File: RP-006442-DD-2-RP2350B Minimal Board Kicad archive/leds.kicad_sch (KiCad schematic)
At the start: 34 parts, among them U10 74HC595, U11 74HC595

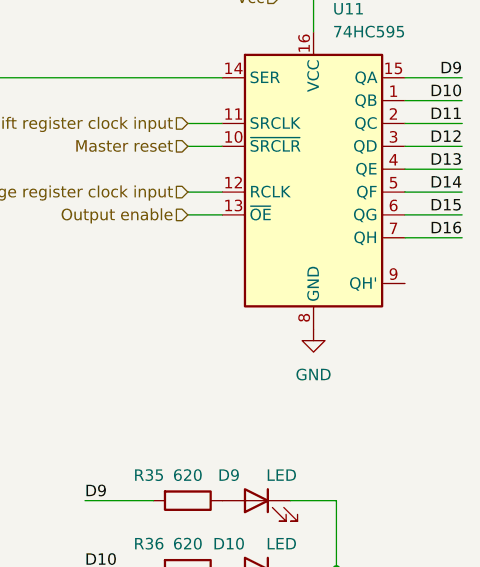
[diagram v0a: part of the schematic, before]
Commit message: Connected GPIOs to Shift Register pins
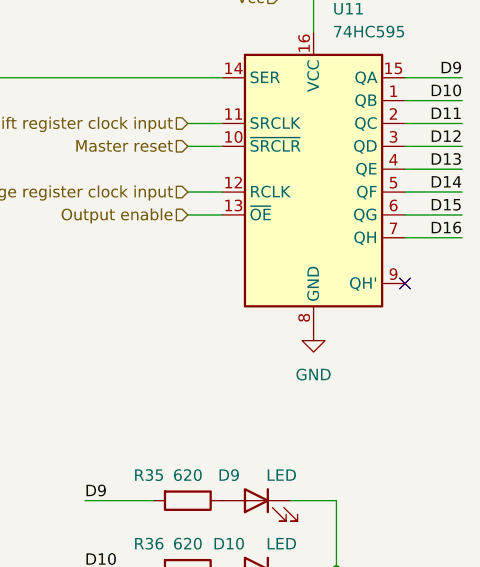
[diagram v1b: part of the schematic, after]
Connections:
- no-connect marks 0 -> 1
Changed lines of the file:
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@@
 		(color 0 0 0 0)
+	)
+	(no_connect
+		(at 162.56 74.93)
 	)
 	(wire

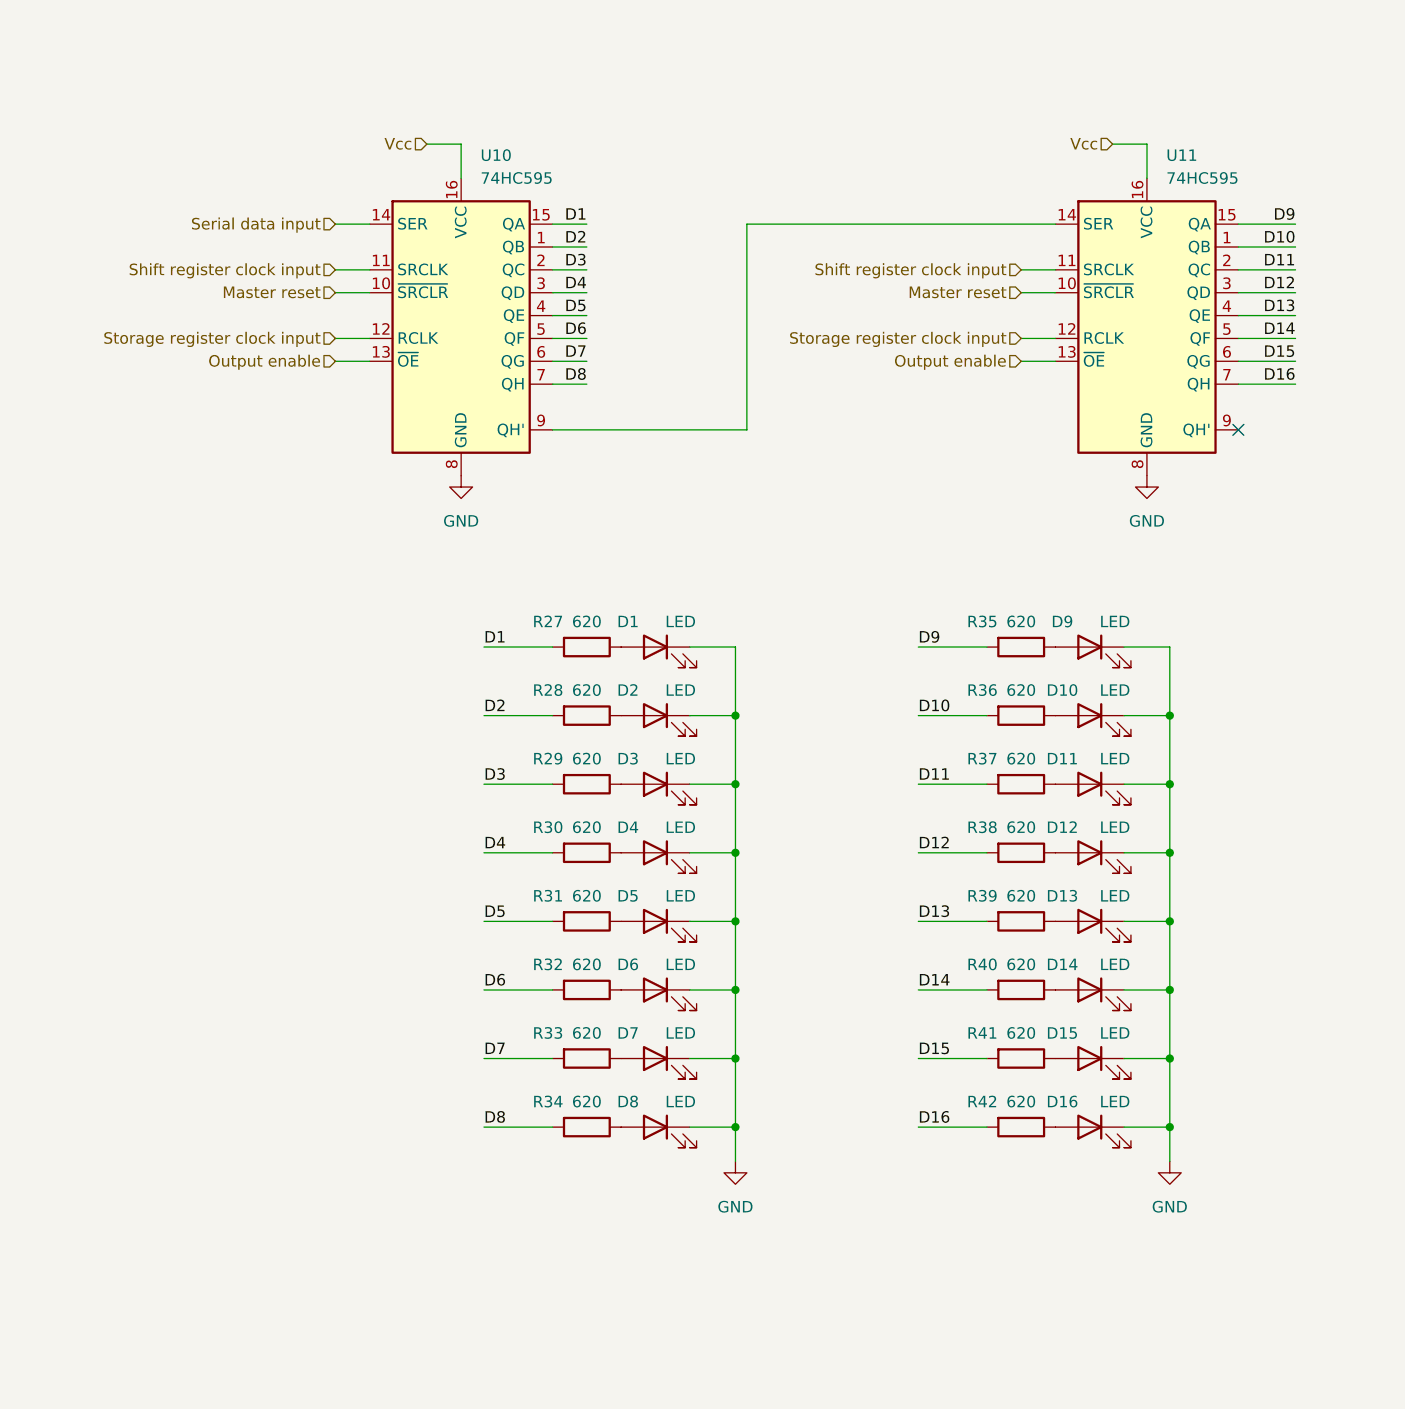
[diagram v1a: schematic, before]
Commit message: Update leds.kicad_sch
Added description text
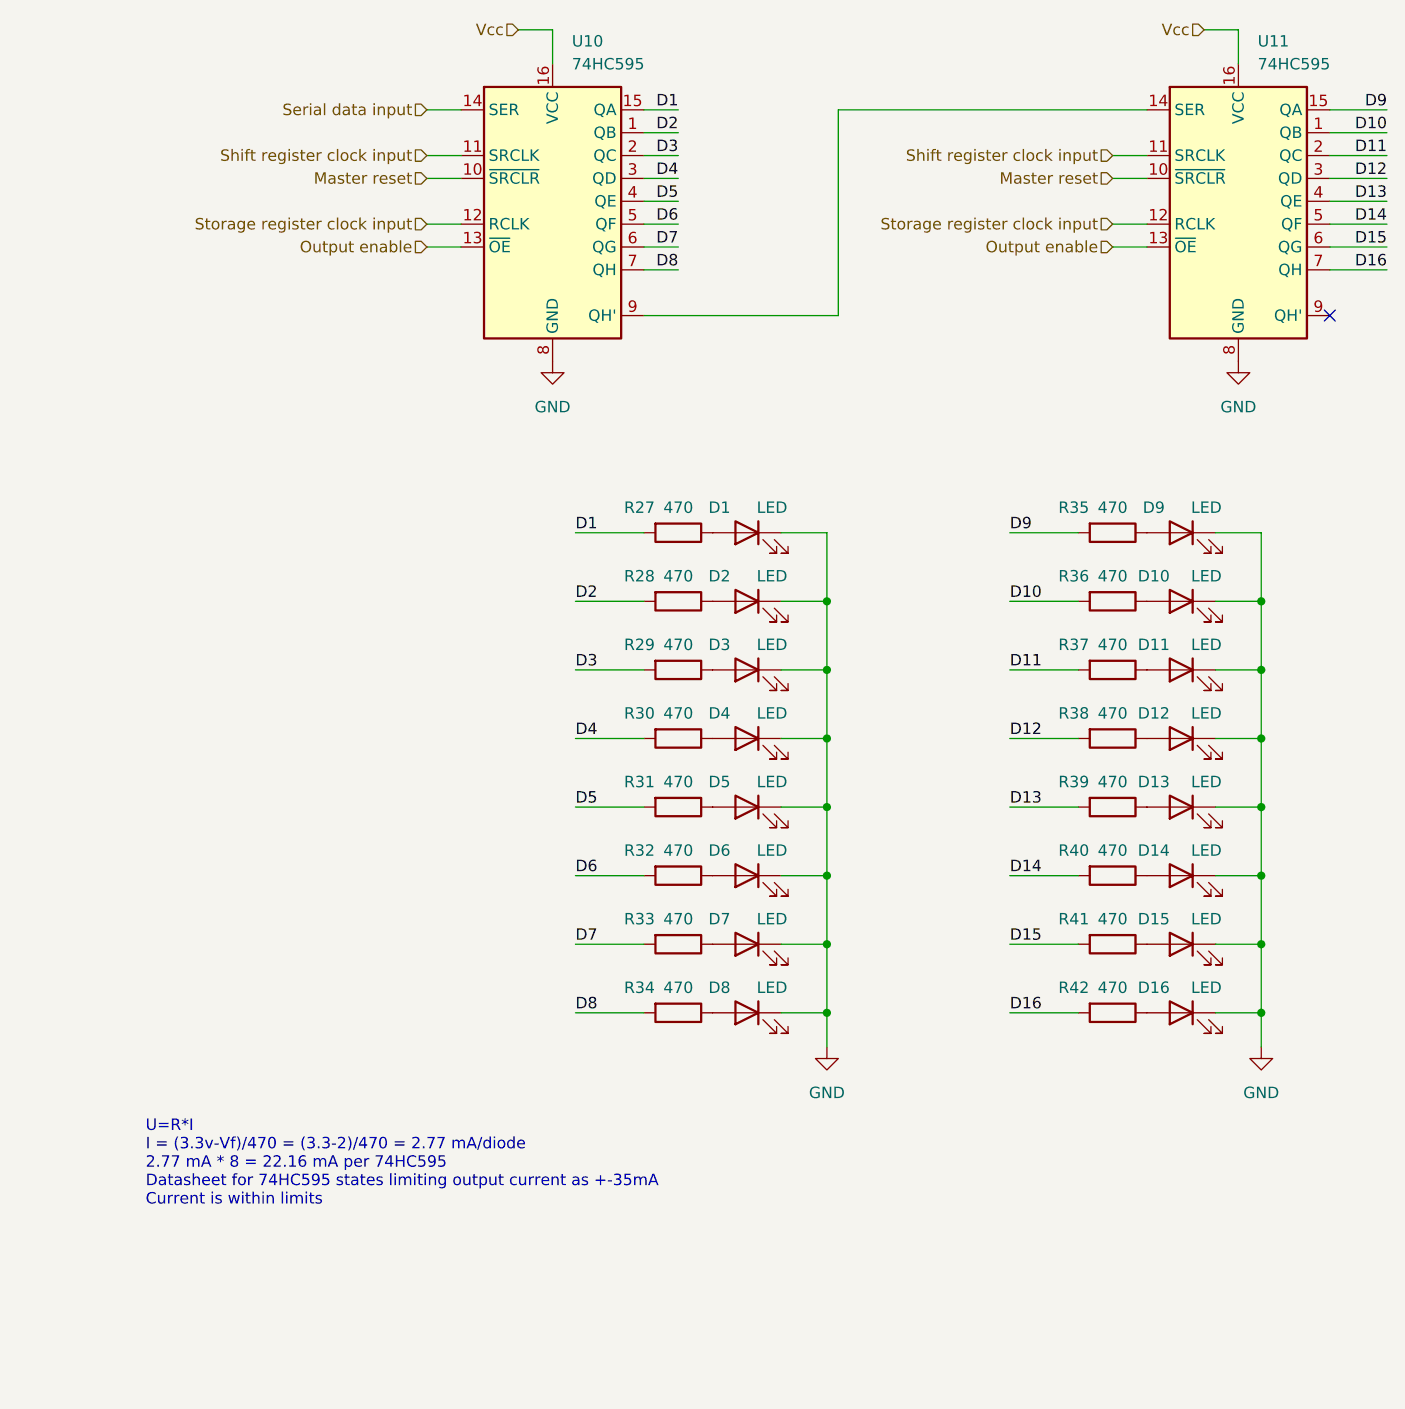
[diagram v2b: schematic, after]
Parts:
- R27, R28, R29, R30, R31, R32, R33, R34, R35, R36, R37, R38, R39, R40, R41, R42: value 620 -> 470; footprint (none) -> Resistor_SMD:R_0402_1005Metric
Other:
- note added: "U=R*I I = (3.3v-Vf)/470 = (3.3-2)/470 = 2.77 mA/diode 2.77 mA * 8 = 22.16 mA per 74HC595 Datasheet for 74HC595 states limiting output current as +-35mA Current is within limits"
- moved on the sheet: D1, D10, D11, D12, D13, D14, D15, D16, D2, D3, D4, D5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

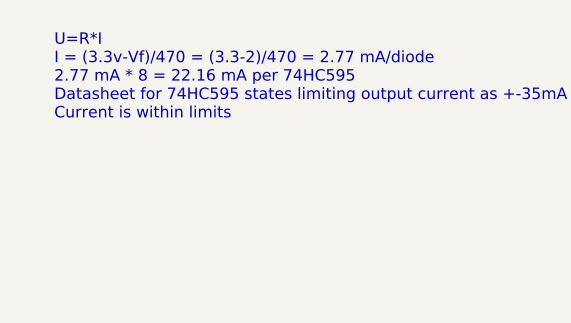
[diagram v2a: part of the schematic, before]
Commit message: Update to schematic and pcb
Changed ht16k33 package from 28SOP to 24SSOP

Placed pcb footprints
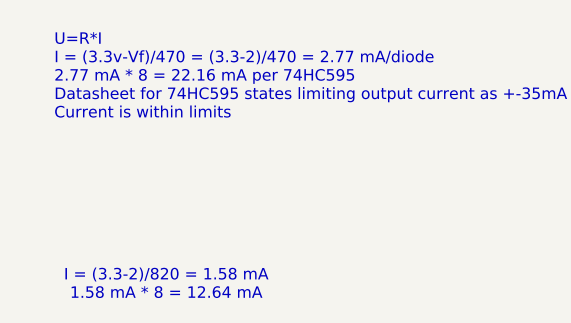
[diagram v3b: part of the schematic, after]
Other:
- note added: "I = (3.3-2)/820 = 1.58 mA 1.58 mA * 8 = 12.64 mA"
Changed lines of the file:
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@@
 	(generator_version "9.0")
 	(paper "A4")
+	(text "I = (3.3-2)/820 = 1.58 mA\n1.58 mA * 8 = 12.64 mA\n"
+		(exclude_from_sim no)
+		(at 53.594 179.578 0)
+		(effects
+			(font
+				(size 1.27 1.27)
+			)
+		)
+	)
 	(text "U=R*I\nI = (3.3v-Vf)/470 = (3.3-2)/470 = 2.77 mA/diode\n2.77 mA * 8 = 22.16 mA per 74HC595\nDatasheet for 74HC595 states limiting output current as +-35mA\nCurrent is within limits"
 		(exclude_from_sim no)

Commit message: text
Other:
- note added: "Foshan NationStar Optoelectronics 25mA Colorless transparent lens 67mcd~195mcd -30℃~+85℃ 615nm~630nm Individual diode Red 130° 65mW 1.6V~2.6V 0805 LED Indication - Discrete ROHS"
- note added: "Texas Instruments SN74HC595DR 8 2V~6V 1 Serial to serial or parallel SOIC-16 Shift Registers ROHS"
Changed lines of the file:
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@@
 	(generator_version "9.0")
 	(paper "A4")
+	(text "Texas Instruments\nSN74HC595DR\n8 2V~6V 1 Serial to serial or parallel \nSOIC-16 Shift Registers ROHS"
+		(exclude_from_sim no)
+		(at 64.77 66.04 0)
+		(effects
+			(font
+				(size 1.27 1.27)
+			)
+		)
+	)
 	(text "I = (3.3-2)/820 = 1.58 mA\n1.58 mA * 8 = 12.64 mA\n"
 		(exclude_from_sim no)
 		(at 53.594 179.578 0)
+		(effects
+			(font
+				(size 1.27 1.27)
+			)
+		)
+	)
+	(text "Foshan NationStar Optoelectronics\n25mA Colorless transparent lens 67mcd~195mcd -30℃~+85℃ \n615nm~630nm Individual diode Red 130° 65mW 1.6V~2.6V \n0805 LED Indication - Discrete ROHS"
+		(exclude_from_sim no)
+		(at 83.82 146.05 0)
 		(effects
 			(font
@@
 			)
 		)
-		(property "Datasheet" "~"
+		(property "Datasheet" "https://jlcpcb.com/api/file/downloadByFileSystemAccessId/8550724080677908480"
 			(at 107.95 86.36 0)
 			(effects

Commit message: Update leds.kicad_sch
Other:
- note added: "74HC595; 74HCT595 Nexperia"
- note removed: "Texas Instruments SN74HC595DR 8 2V~6V 1 Serial to serial or parallel SOIC-16 Shift Registers ROHS"
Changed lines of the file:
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@@
 	(generator_version "9.0")
 	(paper "A4")
-	(text "Texas Instruments\nSN74HC595DR\n8 2V~6V 1 Serial to serial or parallel \nSOIC-16 Shift Registers ROHS"
+	(text "74HC595; 74HCT595\nNexperia\n"
 		(exclude_from_sim no)
 		(at 64.77 66.04 0)
@@
 			)
 		)
-		(property "Datasheet" "http://www.ti.com/lit/ds/symlink/sn74hc595.pdf"
+		(property "Datasheet" "https://jlcpcb.com/api/file/downloadByFileSystemAccessId/8579708624672903168"
 			(at 86.36 49.53 0)
 			(effects
